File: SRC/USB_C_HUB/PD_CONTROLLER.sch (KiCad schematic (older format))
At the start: 40 parts

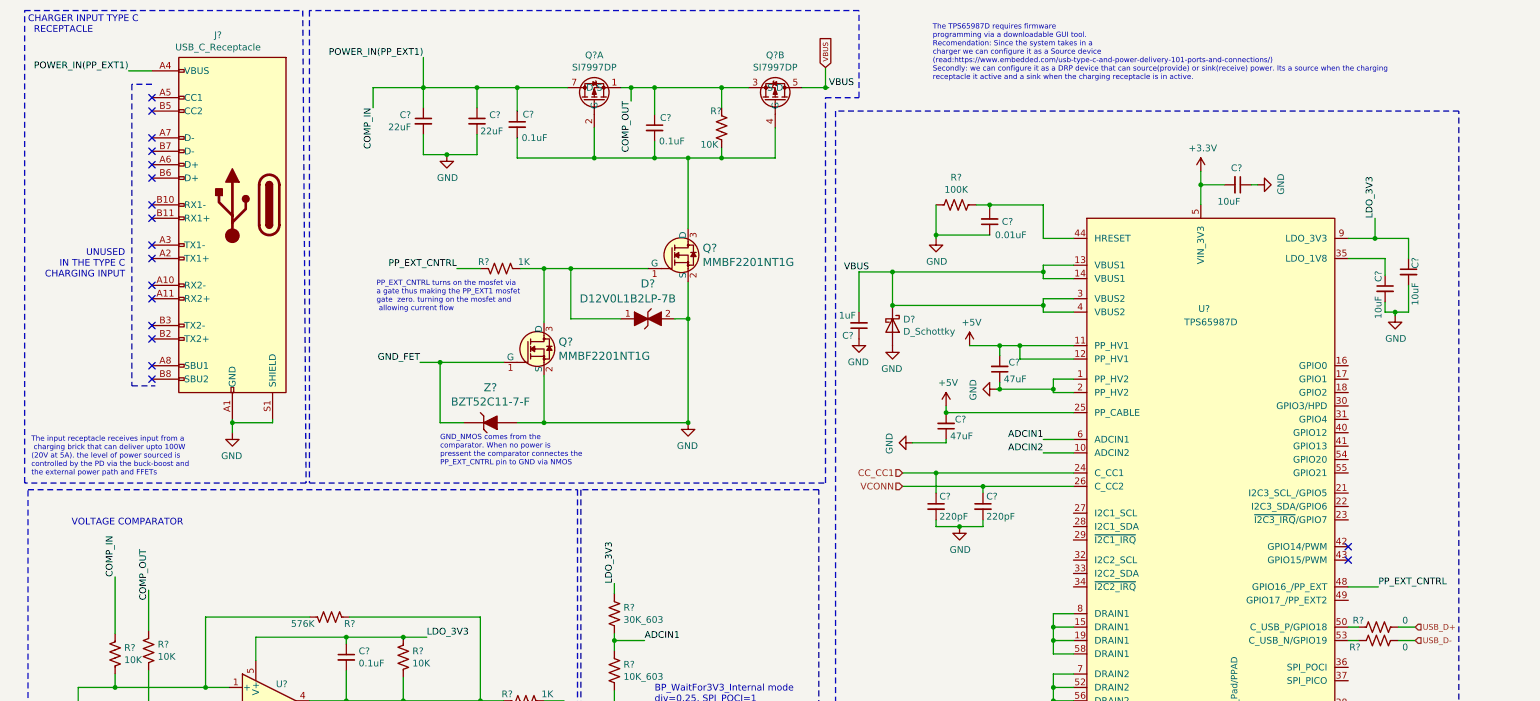
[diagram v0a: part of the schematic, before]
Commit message: PD controller + variable voltage source input(will handle voltage requestvia PD)
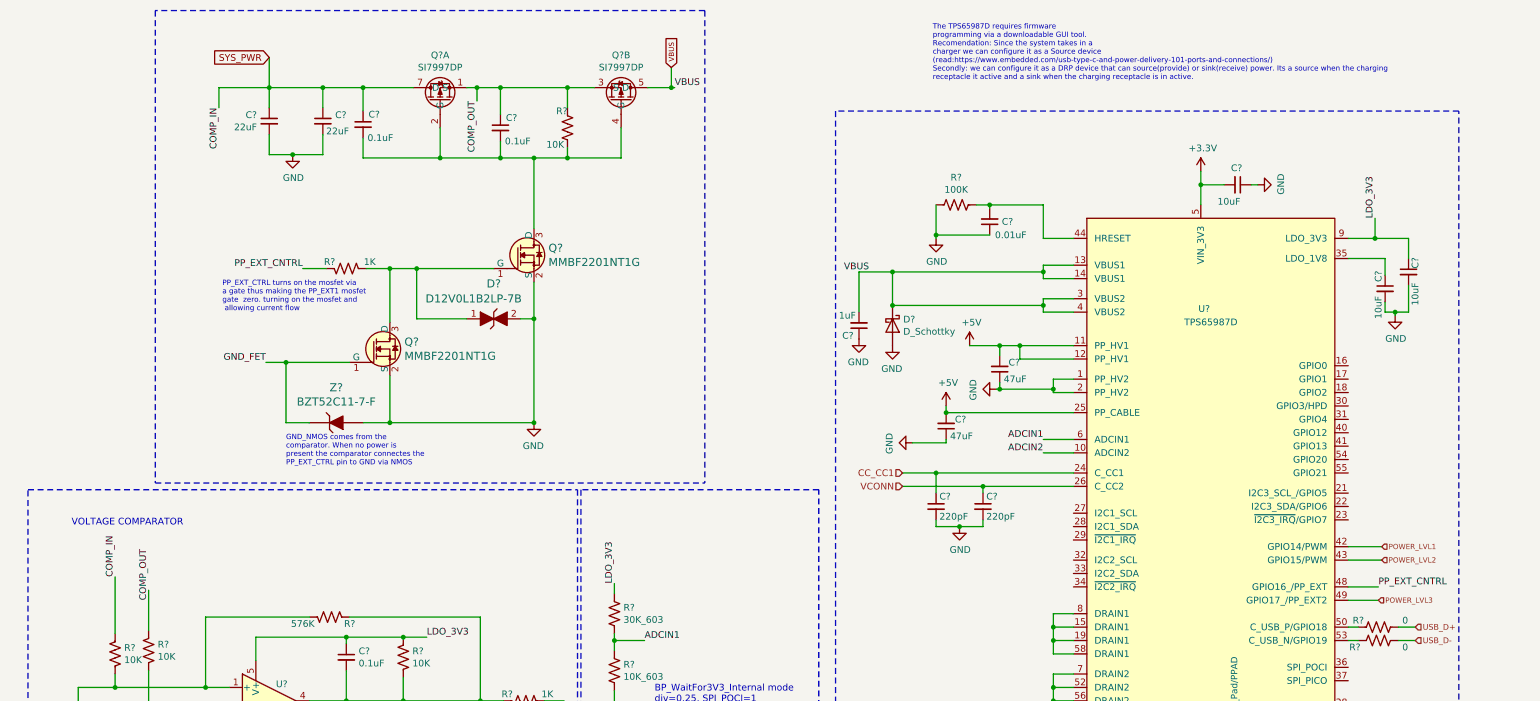
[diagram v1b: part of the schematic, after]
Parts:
- removed J?: USB_C_Receptacle, symbol Connector:USB_C_Receptacle
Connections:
- net POWER_LVL1: now reaches U?.42 (GPIO14/PWM)
- net POWER_LVL2: now reaches U?.43 (GPIO15/PWM)
- net POWER_LVL3: now reaches U?.49 (GPIO17_/PP_EXT2)
- net COMP_IN renamed SYS_PWR
- no-connect marks 18 -> 0
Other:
- note added: "GND_NMOS comes from the \ncomparator. When no power is \npresent the comparator connectes the \nPP_EXT_CTRL pin to GND via NMOS"
- note added: "PP_EXT_CTRL turns on the mosfet via \na gate thus making the PP_EXT1 mosfet\ngate zero. turning on the mosfet and\n allowing current flow"
- note removed: "CHARGER INPUT TYPE C\n RECEPTACLE"
- note removed: "GND_NMOS comes from the \ncomparator. When no power is \npressent the comparator connectes the \nPP_EXT_CNTRL pin to GND via NMOS"
- note removed: "PP_EXT_CNTRL turns on the mosfet via \na gate thus making the PP_EXT1 mosfet\ngate zero. turning on the mosfet and\n allowing current flow"
- note removed: "The input receptacle receives input from a\n charging brick that can deliver upto 100W\n(20V at 5A). the level of power sourced is \ncontrolled by the PD via the buck-boost and \nthe external power path and FFETs"
- note removed: "UNUSED \nIN THE TYPE C \nCHARGING INPUT"
- moved on the sheet: C?, D?, Q?, Q?A, Q?B, R?, Z?

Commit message: With ST PD controller(sink)100W
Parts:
- removed C? (x2): 22uF, symbol Device:C_Small
- removed C? (x3): 0.1uF, symbol Device:C_Small
- removed D?: D12V0L1B2LP-7B, Diode_SMD:D_01005_0402Metric, symbol dk_TVS-Diodes:PGB1010603MR
- removed Q? (x2): SI7997DP, symbol usb_hub:SI7997DP
- removed Q? (x2): MMBF2201NT1G, digikey-footprints:SOT-323, symbol dk_Transistors-FETs-MOSFETs-Single:2N7002P_215
- removed R? (x6): 10K, symbol Device:R_US
- removed R?: 576K, symbol Device:R_US
- removed R? (x2): 1K, symbol Device:R_US
- removed U?: TLV1701AIDBVR, Package_TO_SOT_SMD:SOT-23-5, symbol Amplifier_Operational:TLV172IDCK
- removed Z?: BZT52C11-7-F, digikey-footprints:SOD-123, symbol dk_Diodes-Zener-Single:MMSZ5231B-7-F
- added C?: 1nF, symbol Device:C
- added C?: 0.1uF, symbol Device:C
- added C? (x2): 22uF, symbol Device:C
- added C? (x2): 100pF, symbol Device:C
- added D? (x3): SMAJ30A, Diode_SMD:D_SMB, symbol Diode:SM6T30A
- added D?: ESDA25P35, digikey-footprints:SOD-523, symbol dk_TVS-Diodes:ESD5Z3_3T1G
- added L?: 10uH, symbol OLIMEX_RCL:INDUCTOR_SMALL
- added Q? (x3): BSH105,215, Package_TO_SOT_SMD:SC-59, symbol dk_Transistors-FETs-MOSFETs-Single:2N7002P_215
- added R?: 270, symbol Device:R_US
- added R?: 47.5K, symbol Device:R_US
- added R? (x4): 100K, symbol Device:R_US
- added R?: 11K, symbol Device:R_US
- added R?: 30K, symbol Device:R_US
- added R?: 9.53K, symbol Device:R_US
- added R?: 8.87K_603, symbol Device:R_US
- added R?: 3.65K_603, symbol Device:R_US
- added R?: 2.2K_805, symbol Device:R_US
- added U?: CWDM3011P, symbol usb_hub:CWDM3011P
- added U?: LM3489QMM, symbol usb_hub:LM3489QMM
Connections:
- net GND: now also C?.2, C?.2, C?.2, D?.2 (A2), D?.2 (A2), D?.2 (A2), D?.A, R?.2, U?.2 (GND), U?.6 (PGND)
- net POWER_LVL1: now also Q?.1 (G), R?.1
- net POWER_LVL2: now also Q?.1 (G), R?.1
- net POWER_LVL3: now also Q?.1 (G), R?.1
- net SYS_PWR: now also C?.1, C?.1, C?.1, C?.1, D?.1 (A1), D?.1 (A1), D?.1 (A1), R?.1, R?.1, U?.1 (S), U?.2 (S), U?.3 (S), U?.8 (VIN)
- new net: U?.1 (S), U?.7 (PGATE)
- new net: D?.K, L?.1, R?.1, U?.6 (D), U?.7 (D), U?.8 (D)
- new net: R?.2, U?.1 (ISENSE)
- new net: C?.2, R?.2, U?.5 (ADJ)
- new net: R?.1, R?.2, U?.3 (EN)
- new net: C?.1, L?.2, R?.1
- new net: Q?.2 (S), R?.1 (x3)
- new net: C?.1, C?.2, Q?.3 (D), Q?.3 (D), Q?.3 (D), R?.1, R?.2, U?.4 (FB)
- new net: C?.2, R?.2, R?.2, R?.2, R?.2, R?.2, R?.2, R?.2
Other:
- note added: "FEEDBACK PATH\n(USED TO SET THE DESIRED VOLTAGE)"
- note added: "VARIABLE VOLTAGE PROVIDER(SOURCE)"
- note removed: "GND_NMOS comes from the \ncomparator. When no power is \npresent the comparator connectes the \nPP_EXT_CTRL pin to GND via NMOS"
- note removed: "PP_EXT_CTRL turns on the mosfet via \na gate thus making the PP_EXT1 mosfet\ngate zero. turning on the mosfet and\n allowing current flow"
- note removed: "VOLTAGE COMPARATOR"
- moved on the sheet: C?, D?, R?, U?
